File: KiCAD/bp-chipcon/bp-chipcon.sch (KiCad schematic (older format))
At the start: 38 parts, among them J1 audio_out, J2 video_out, M1 BLUE_PILL, Q1 2N3904, Q2 2N3906, SW1 power, SW2 A, SW3 UP, SW4 RIGHT, SW5 LEFT, SW6 B, SW7 DOWN, U1 74HC86N

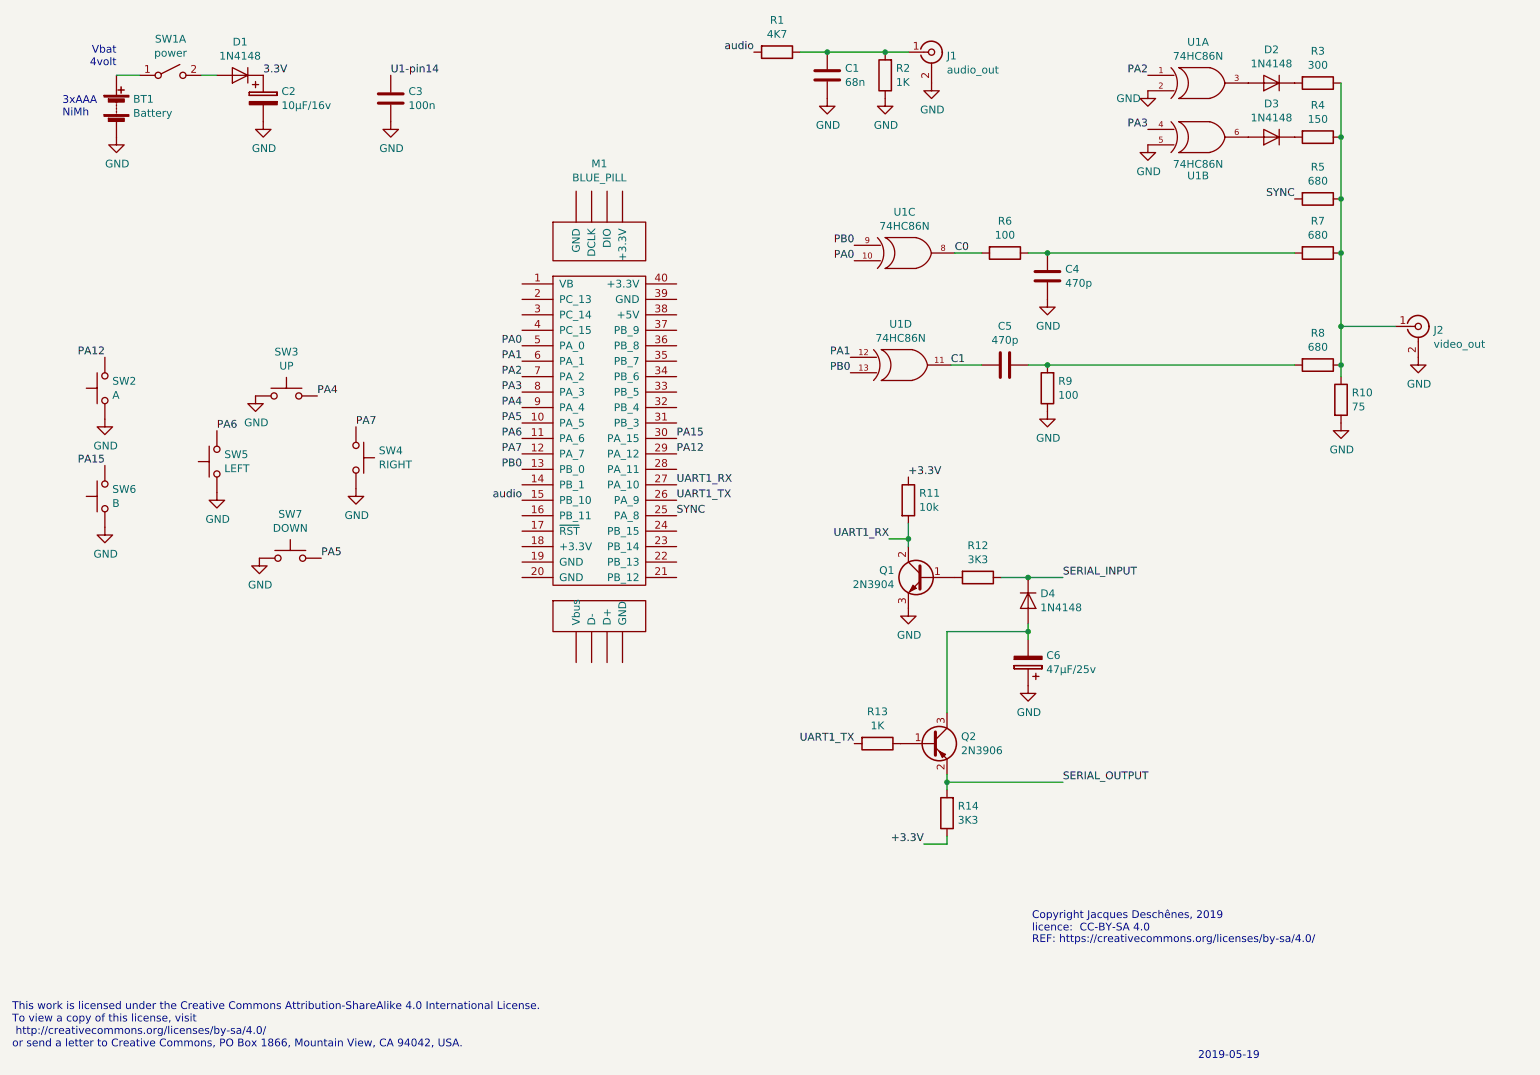
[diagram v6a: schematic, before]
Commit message: Modified schematic added keypad sheet
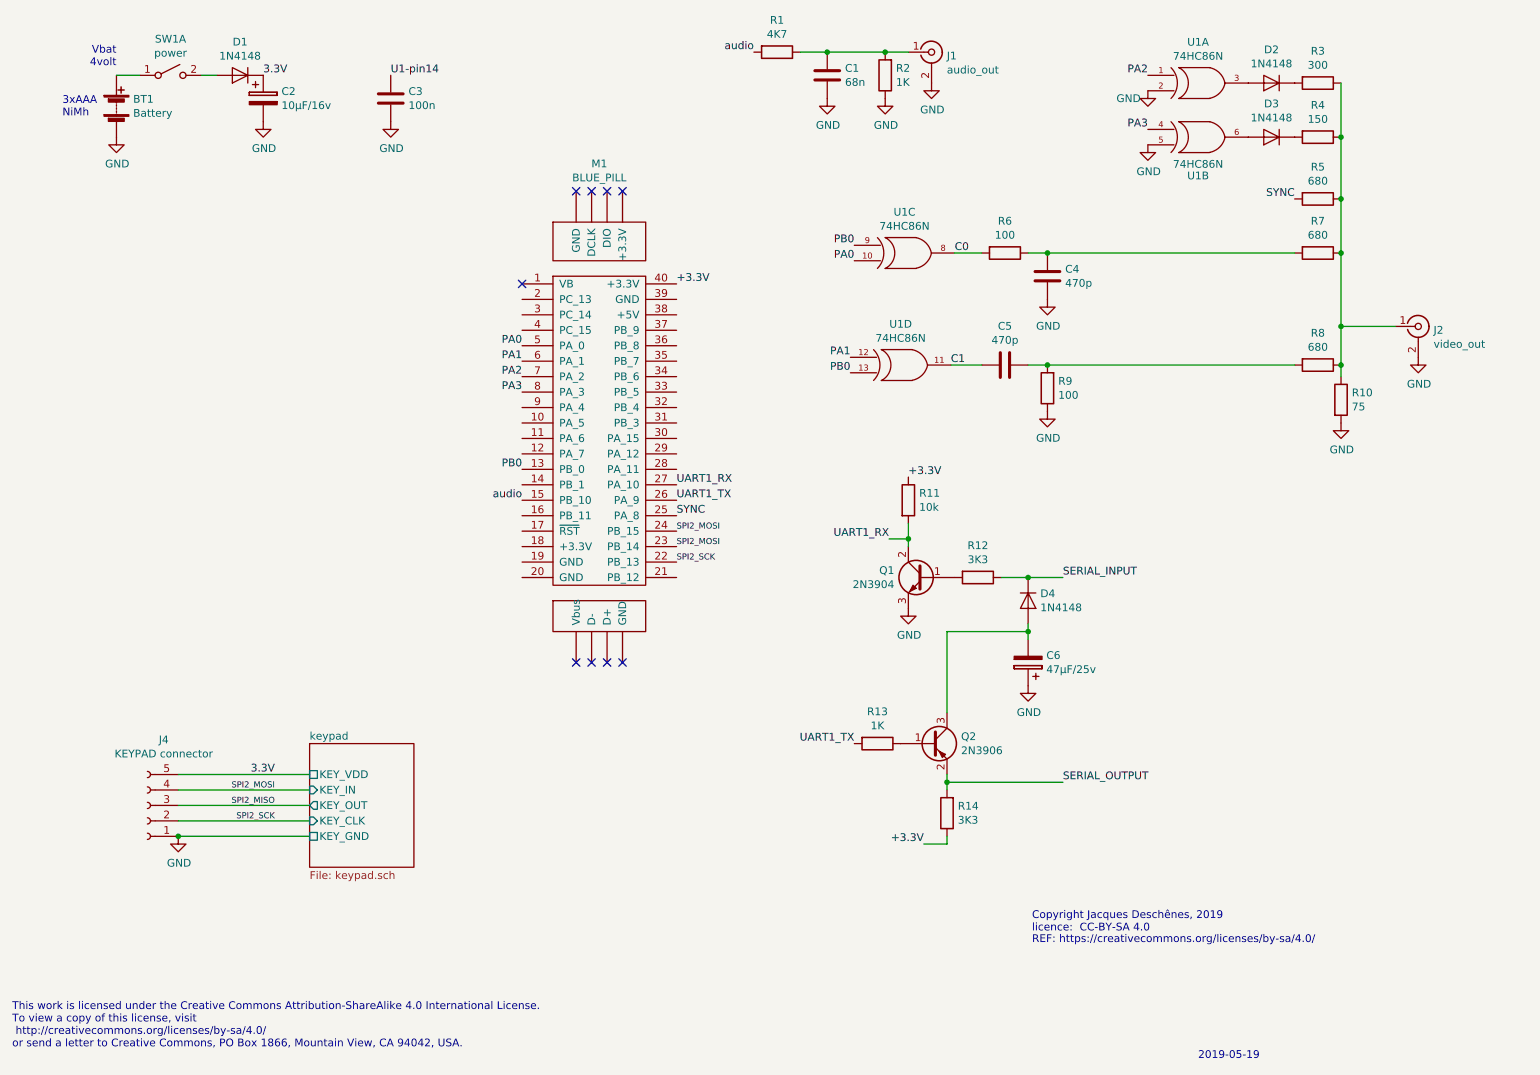
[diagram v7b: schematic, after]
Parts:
- removed SW2: A, symbol switches:SW_Push
- removed SW3: UP, symbol switches:SW_Push
- removed SW4: RIGHT, symbol switches:SW_Push
- removed SW5: LEFT, symbol switches:SW_Push
- removed SW6: B, symbol switches:SW_Push
- removed SW7: DOWN, symbol switches:SW_Push
- added J4: KEYPAD connector, symbol conn:Conn_01x05_Female
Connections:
- net +3.3V: now also M1.40 (+3.3V)
- net 3.3V: now also J4.5 (Pin_5)
- net GND: now also J4.1 (Pin_1)
- net SPI2_SCK: now reaches M1.22 (PB_13)
- net SPI2_SCK: now also J4.2 (Pin_2)
- net SPI2_MOSI: now reaches M1.23 (PB_14)
- net SPI2_MOSI: now also M1.24 (PB_15), J4.4 (Pin_4)
- net PA12: no longer names the net of M1.29 (PA_12)
- net PA15: no longer names the net of M1.30 (PA_15)
- net PA4: no longer names the net of M1.9 (PA_4)
- net PA5: no longer names the net of M1.10 (PA_5)
- net PA6: no longer names the net of M1.11 (PA_6)
- net PA7: no longer names the net of M1.12 (PA_7)
- new net SPI2_MISO: J4.3 (Pin_3)
- no-connect marks 0 -> 9
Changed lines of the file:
@@
 $Descr A4 11693 8268
 encoding utf-8
-Sheet 1 1
+Sheet 1 2
 Title ""
 Date ""
@@
 Text Label 3825 3300 2    50   ~ 0
 PA3
-Text Label 3825 3400 2    50   ~ 0
-PA4
-Text Label 3825 3500 2    50   ~ 0
-PA5
-Text Label 3825 3600 2    50   ~ 0
-PA6
-Text Label 3825 3700 2    50   ~ 0
-PA7
 $Comp
 L device:C C3
@@
 	1    0    0    -1
 $EndComp
-$Comp
-L switches:SW_Push SW5
-U 1 1 5CD8B847
-P 1850 3750
-F 0 "SW5" V 1896 3702 50  0000 R CNN
-F 1 "LEFT" V 1805 3702 50  0000 R CNN
-F 2 "" H 1850 3950 50  0001 C CNN
-F 3 "" H 1850 3950 50  0001 C CNN
-	1    1850 3750
-	0    -1   -1   0
-$EndComp
-$Comp
-L switches:SW_Push SW4
-U 1 1 5CD8BEE3
-P 2750 3725
-F 0 "SW4" V 2704 3873 50  0000 L CNN
-F 1 "RIGHT" V 2795 3873 50  0000 L CNN
-F 2 "" H 2750 3925 50  0001 C CNN
-F 3 "" H 2750 3925 50  0001 C CNN
-	1    2750 3725
-	0    1    1    0
-$EndComp
-$Comp
-L switches:SW_Push SW3
-U 1 1 5CD8BFBD
-P 2300 3325
-F 0 "SW3" H 2300 3610 50  0000 C CNN
-F 1 "UP" H 2300 3519 50  0000 C CNN
-F 2 "" H 2300 3525 50  0001 C CNN
-F 3 "" H 2300 3525 50  0001 C CNN
-	1    2300 3325
-	1    0    0    -1
-$EndComp
-$Comp
-L switches:SW_Push SW7
-U 1 1 5CD8C0BD
-P 2325 4375
-F 0 "SW7" H 2325 4660 50  0000 C CNN
-F 1 "DOWN" H 2325 4569 50  0000 C CNN
-F 2 "" H 2325 4575 50  0001 C CNN
-F 3 "" H 2325 4575 50  0001 C CNN
-	1    2325 4375
-	1    0    0    -1
-$EndComp
-$Comp
-L power:GND #PWR011
-U 1 1 5CD8C153
-P 2100 3325
-F 0 "#PWR011" H 2100 3075 50  0001 C CNN
-F 1 "GND" H 2105 3152 50  0000 C CNN
-F 2 "" H 2100 3325 50  0001 C CNN
-F 3 "" H 2100 3325 50  0001 C CNN
-	1    2100 3325
-	1    0    0    -1
-$EndComp
-$Comp
-L power:GND #PWR018
-U 1 1 5CD8C19E
-P 2125 4375
-F 0 "#PWR018" H 2125 4125 50  0001 C CNN
-F 1 "GND" H 2130 4202 50  0000 C CNN
-F 2 "" H 2125 4375 50  0001 C CNN
-F 3 "" H 2125 4375 50  0001 C CNN
-	1    2125 4375
-	1    0    0    -1
-$EndComp
-$Comp
-L power:GND #PWR016
-U 1 1 5CD8C2D3
-P 1850 3950
-F 0 "#PWR016" H 1850 3700 50  0001 C CNN
-F 1 "GND" H 1855 3777 50  0000 C CNN
-F 2 "" H 1850 3950 50  0001 C CNN
-F 3 "" H 1850 3950 50  0001 C CNN
-	1    1850 3950
-	1    0    0    -1
-$EndComp
-$Comp
-L power:GND #PWR015
-U 1 1 5CD8C31E
-P 2750 3925
-F 0 "#PWR015" H 2750 3675 50  0001 C CNN
-F 1 "GND" H 2755 3752 50  0000 C CNN
-F 2 "" H 2750 3925 50  0001 C CNN
-F 3 "" H 2750 3925 50  0001 C CNN
-	1    2750 3925
-	1    0    0    -1
-$EndComp
-$Comp
-L switches:SW_Push SW2
-U 1 1 5CD8C684
-P 1125 3275
-F 0 "SW2" V 1171 3227 50  0000 R CNN
-F 1 "A" V 1080 3227 50  0000 R CNN
-F 2 "" H 1125 3475 50  0001 C CNN
-F 3 "" H 1125 3475 50  0001 C CNN
-	1    1125 3275
-	0    -1   -1   0
-$EndComp
-$Comp
-L switches:SW_Push SW6
-U 1 1 5CD8C71E
-P 1125 3975
-F 0 "SW6" V 1171 3927 50  0000 R CNN
-F 1 "B" V 1080 3927 50  0000 R CNN
-F 2 "" H 1125 4175 50  0001 C CNN
-F 3 "" H 1125 4175 50  0001 C CNN
-	1    1125 3975
-	0    -1   -1   0
-$EndComp
-$Comp
-L power:GND #PWR013
-U 1 1 5CD8C7D2
-P 1125 3475
-F 0 "#PWR013" H 1125 3225 50  0001 C CNN
-F 1 "GND" H 1130 3302 50  0000 C CNN
-F 2 "" H 1125 3475 50  0001 C CNN
-F 3 "" H 1125 3475 50  0001 C CNN
-	1    1125 3475
-	1    0    0    -1
-$EndComp
-$Comp
-L power:GND #PWR017
-U 1 1 5CD8C821
-P 1125 4175
-F 0 "#PWR017" H 1125 3925 50  0001 C CNN
-F 1 "GND" H 1130 4002 50  0000 C CNN
-F 2 "" H 1125 4175 50  0001 C CNN
-F 3 "" H 1125 4175 50  0001 C CNN
-	1    1125 4175
-	1    0    0    -1
-$EndComp
-Text Label 2500 3325 0    50   ~ 0
-PA4
-Text Label 2525 4375 0    50   ~ 0
-PA5
-Text Label 1850 3550 0    50   ~ 0
-PA6
-Text Label 2750 3525 0    50   ~ 0
-PA7
-Text Label 4825 3600 0    50   ~ 0
-PA15
-Text Label 4825 3700 0    50   ~ 0
-PA12
-Text Label 1125 3075 2    50   ~ 0
-PA12
-Text Label 1125 3775 2    50   ~ 0
-PA15
 Wire Wire Line
 	7225 3125 8825 3125
@@
 Text Label 5950 3175 2    50   ~ 0
 PB0
+$Sheet
+S 2450 5575 675  800
+U 5CE41476
+F0 "keypad" 50
+F1 "keypad.sch" 50
+F2 "KEY_VDD" U L 2450 5775 50
+F3 "KEY_GND" U L 2450 6175 50
+F4 "KEY_CLK" I L 2450 6075 50
+F5 "KEY_IN" I L 2450 5875 50
+F6 "KEY_OUT" O L 2450 5975 50
+$EndSheet
+$Comp
+L power:GND #PWR0101
+U 1 1 5CE4EBEB
+P 1600 6175
+F 0 "#PWR0101" H 1600 5925 50  0001 C CNN
+F 1 "GND" H 1605 6002 50  0000 C CNN
+F 2 "" H 1600 6175 50  0001 C CNN
+F 3 "" H 1600 6175 50  0001 C CNN
+	1    1600 6175
+	1    0    0    -1
+$EndComp
+Text Label 2225 5775 2    50   ~ 0
+3.3V
+Text Label 2225 6075 2    39   ~ 0
+SPI2_SCK
+Text Label 2225 5875 2    39   ~ 0
+SPI2_MOSI
+Text Label 2225 5975 2    39   ~ 0
+SPI2_MISO
+Text Label 4825 4200 0    39   ~ 0
+SPI2_MOSI
+Text Label 4825 4300 0    39   ~ 0
+SPI2_MOSI
+Text Label 4825 4400 0    39   ~ 0
+SPI2_SCK
+NoConn ~ 4275 5050
+NoConn ~ 4375 5050
+NoConn ~ 4175 5050
+NoConn ~ 4475 5050
+NoConn ~ 4175 2000
+NoConn ~ 4275 2000
+NoConn ~ 4375 2000
+NoConn ~ 4475 2000
+NoConn ~ 3825 2600
+Text Label 4825 2600 0    50   ~ 0
++3.3V
+$Comp
+L conn:Conn_01x05_Female J4
+U 1 1 5CE593C3
+P 1400 5975
+F 0 "J4" H 1294 5550 50  0000 C CNN
+F 1 "KEYPAD connector" H 1294 5641 50  0000 C CNN
+F 2 "" H 1400 5975 50  0001 C CNN
+F 3 "~" H 1400 5975 50  0001 C CNN
+	1    1400 5975
+	-1   0    0    1
+$EndComp
+Wire Wire Line
+	1600 5875 2450 5875
+Wire Wire Line
+	1600 5775 2450 5775
+Wire Wire Line
+	1600 5975 2450 5975
+Wire Wire Line
+	1600 6075 2450 6075
+Wire Wire Line
+	1600 6175 2450 6175
+Connection ~ 1600 6175
 $EndSCHEMATC

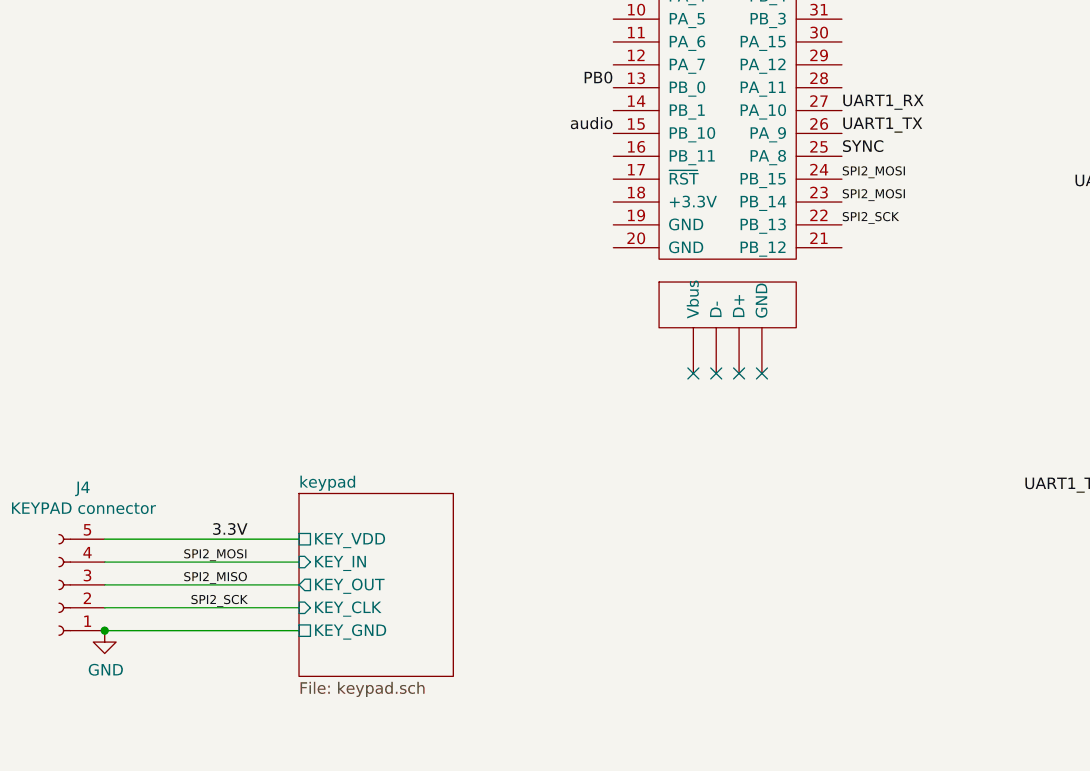
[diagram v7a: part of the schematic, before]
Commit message: Working on TV_OUT_handler gamepad interface added game_timer and sound_timer
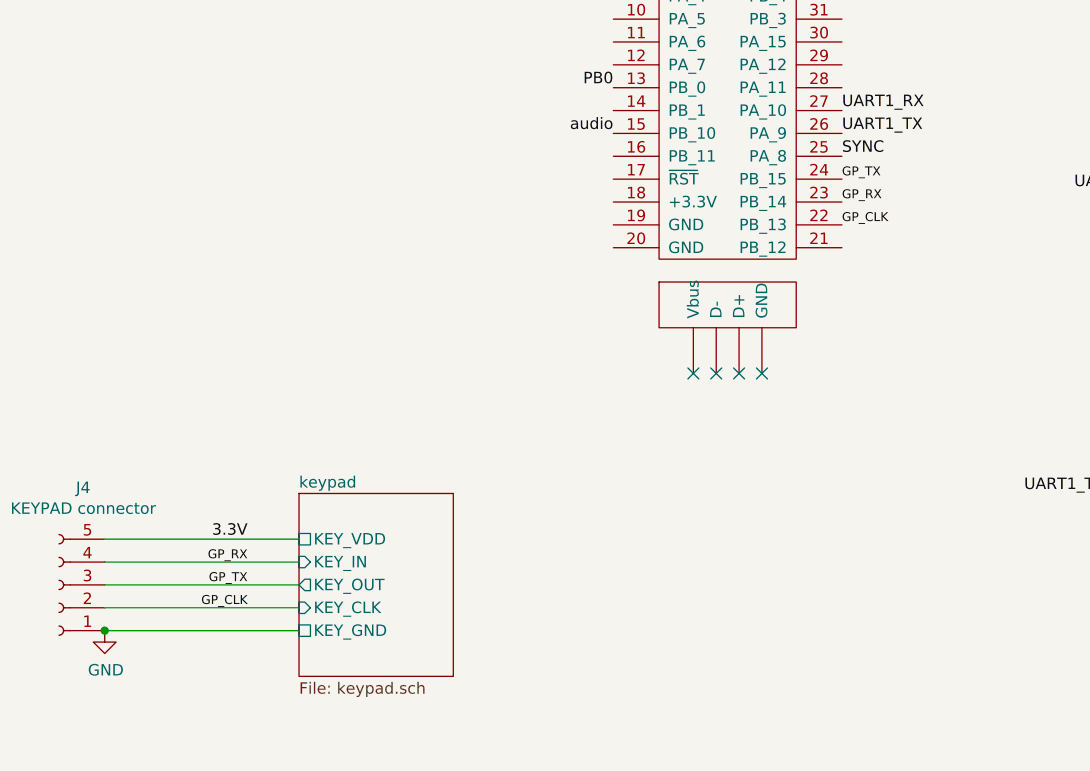
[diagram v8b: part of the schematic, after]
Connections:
- net SPI2_MISO renamed GP_TX
- net GP_TX: now also M1.24 (PB_15)
- net SPI2_MOSI renamed GP_RX
- net GP_RX: no longer M1.24 (PB_15)
- net SPI2_SCK renamed GP_CLK
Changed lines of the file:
@@
 3.3V
 Text Label 2225 6075 2    39   ~ 0
-SPI2_SCK
+GP_CLK
 Text Label 2225 5875 2    39   ~ 0
-SPI2_MOSI
+GP_RX
 Text Label 2225 5975 2    39   ~ 0
-SPI2_MISO
+GP_TX
 Text Label 4825 4200 0    39   ~ 0
-SPI2_MOSI
+GP_TX
 Text Label 4825 4300 0    39   ~ 0
-SPI2_MOSI
+GP_RX
 Text Label 4825 4400 0    39   ~ 0
-SPI2_SCK
+GP_CLK
 NoConn ~ 4275 5050
 NoConn ~ 4375 5050
